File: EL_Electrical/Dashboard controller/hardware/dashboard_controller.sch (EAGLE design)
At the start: 46 parts, among them IC1 MCP2562-E_SN, IC2 MCP2515-I_SO, J1 22-27-2091-09, Q1 BSS138, Q4 BSS138, Q5 BSS138, Q6 BSS138

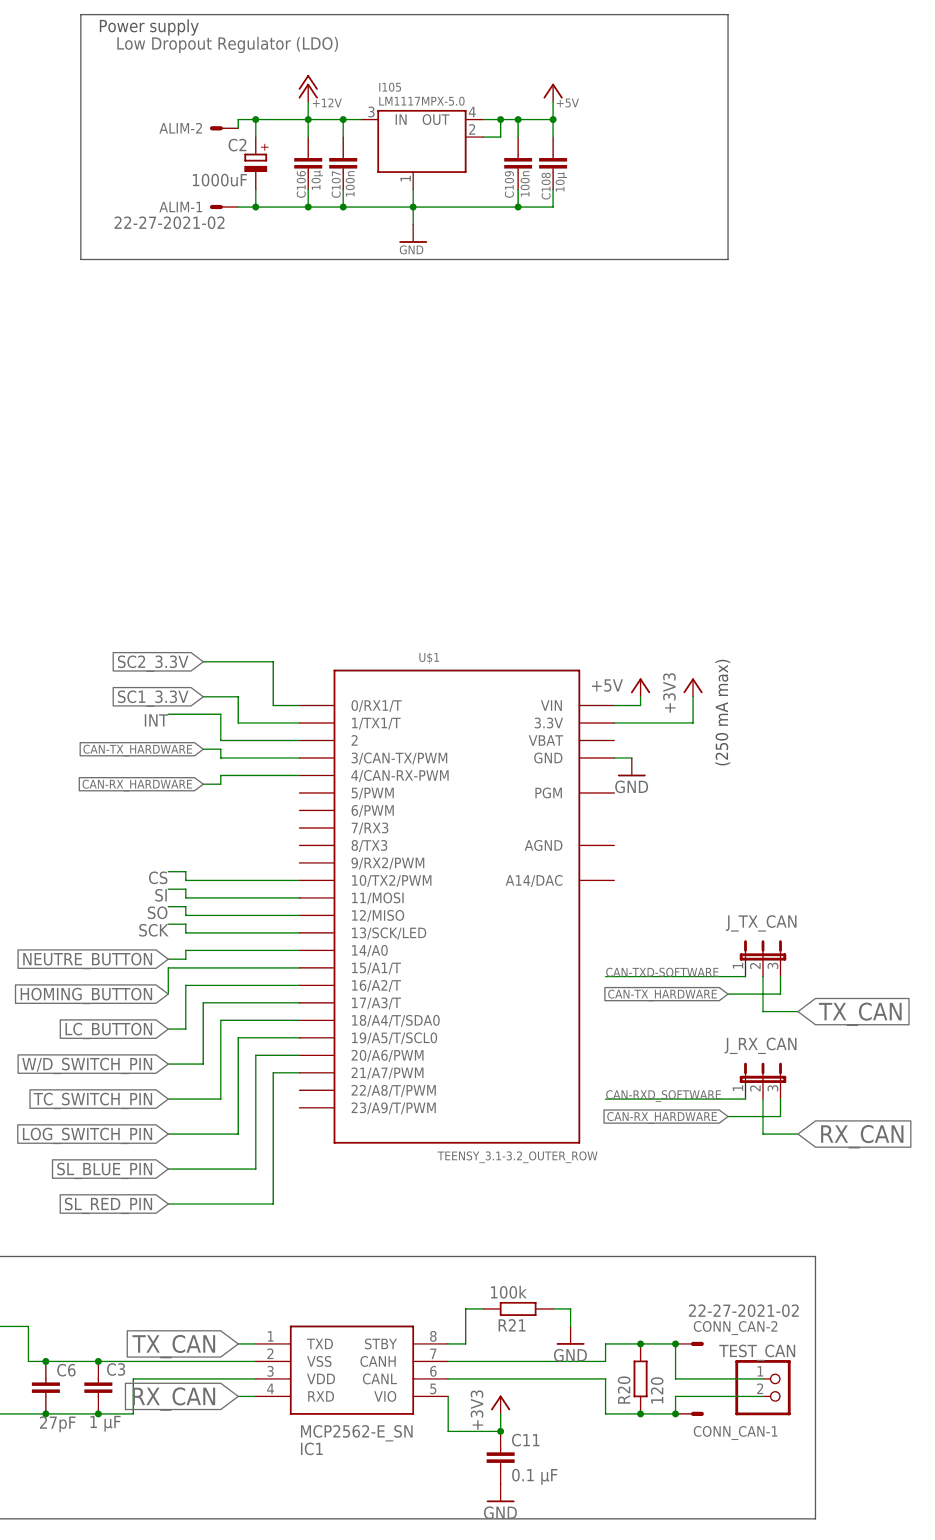
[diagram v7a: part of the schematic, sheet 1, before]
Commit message: Update holes and text
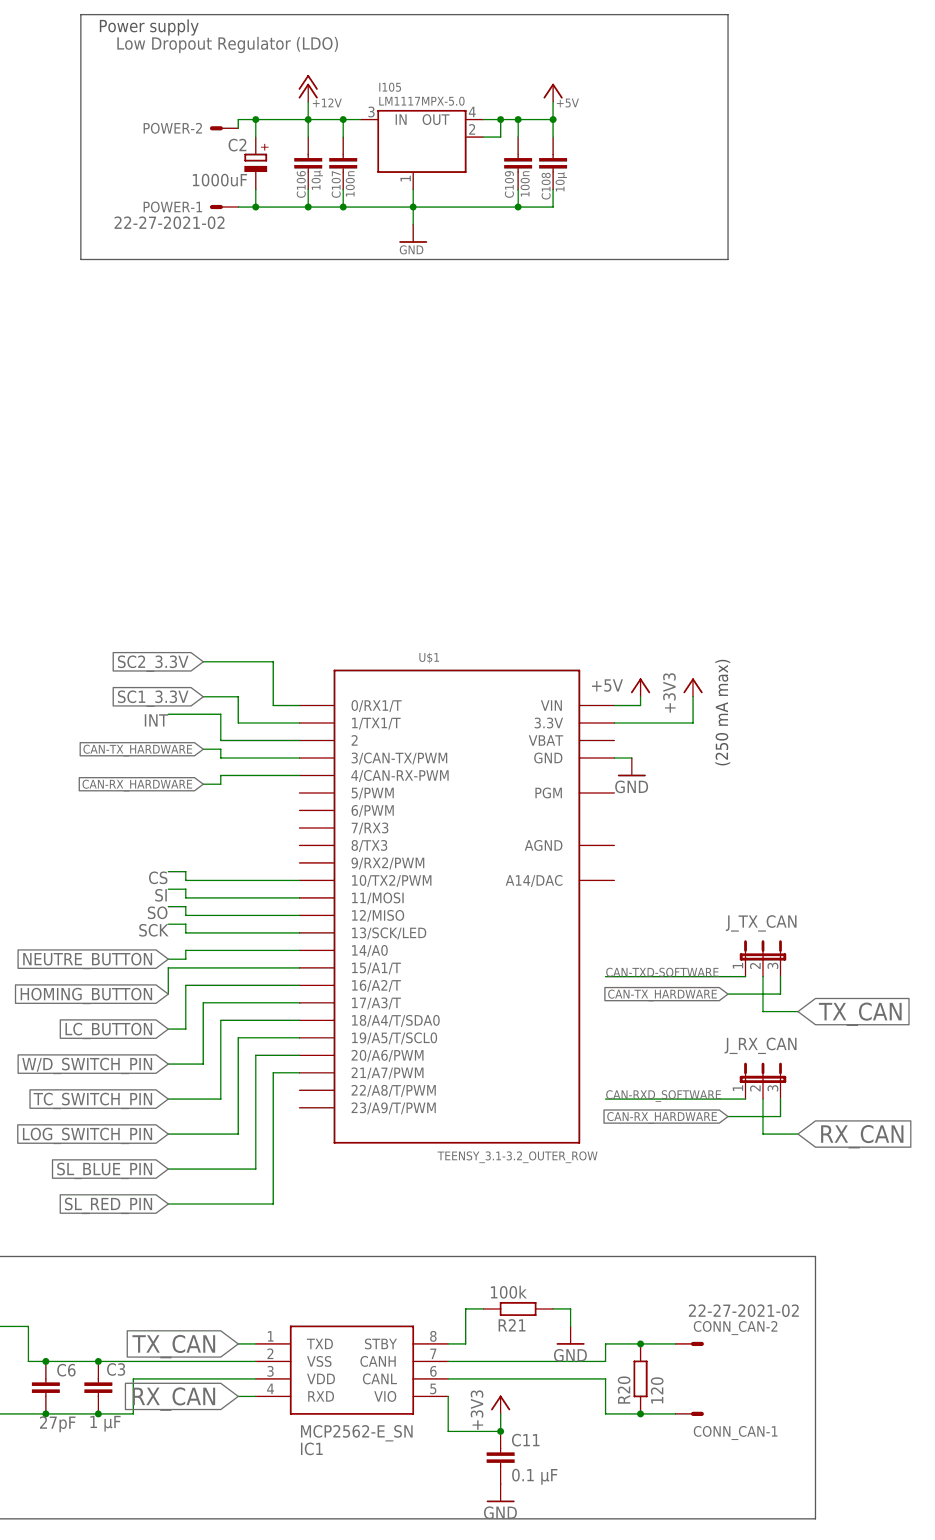
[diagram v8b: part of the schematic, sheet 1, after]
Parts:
- removed TEST_CAN: (no value), test_pin_DTA:PINHD-1X2
- renumbered ALIM to POWER
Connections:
- net N$1: no longer TEST_CAN.1
- net N$6: no longer TEST_CAN.2
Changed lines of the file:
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@@
 <part name="+3V6" library="supply1" library_urn="urn:adsk.eagle:library:371" deviceset="+3V3" device=""/>
 <part name="P+13" library="supply1" library_urn="urn:adsk.eagle:library:371" deviceset="+5V" device=""/>
-<part name="ALIM" library="con-molex" library_urn="urn:adsk.eagle:library:165" deviceset="22-?-02" device="27-2021" package3d_urn="urn:adsk.eagle:package:8078645/1"/>
+<part name="POWER" library="con-molex" library_urn="urn:adsk.eagle:library:165" deviceset="22-?-02" device="27-2021" package3d_urn="urn:adsk.eagle:package:8078645/1"/>
 <part name="R23" library="rcl" library_urn="urn:adsk.eagle:library:334" deviceset="R-EU_" device="R0805" package3d_urn="urn:adsk.eagle:package:23553/2" value="1k"/>
 <part name="+3V1" library="supply1" library_urn="urn:adsk.eagle:library:371" deviceset="+3V3" device=""/>
 <part name="GND" library="pinhead" library_urn="urn:adsk.eagle:library:325" deviceset="PINHD-1X1" device="" package3d_urn="urn:adsk.eagle:package:22485/2"/>
 <part name="GND2" library="supply1" deviceset="GND" device=""/>
-<part name="TEST_CAN" library="test_pin_DTA" deviceset="PINHD-1X2" device="" package3d_urn="urn:adsk.eagle:package:22435/2"/>
 <part name="Q1" library="transistor-small-signal" library_urn="urn:adsk.eagle:library:401" deviceset="BSS123" device="" package3d_urn="urn:adsk.eagle:package:28738/2" value="BSS138"/>
 <part name="R1" library="rcl" library_urn="urn:adsk.eagle:library:334" deviceset="R-EU_" device="R0805" package3d_urn="urn:adsk.eagle:package:23553/2" value="10k"/>
@@
 <attribute name="VALUE" x="190.5" y="200.66" size="1.778" layer="96" rot="R180"/>
 </instance>
-<instance part="ALIM" gate="-1" x="48.26" y="195.58" smashed="yes" rot="R180">
+<instance part="POWER" gate="-1" x="48.26" y="195.58" smashed="yes" rot="R180">
 <attribute name="NAME" x="45.72" y="196.342" size="1.524" layer="95" rot="R180"/>
 <attribute name="VALUE" x="49.022" y="194.183" size="1.778" layer="96" rot="R180"/>
 </instance>
-<instance part="ALIM" gate="-2" x="48.26" y="207.01" smashed="yes" rot="R180">
+<instance part="POWER" gate="-2" x="48.26" y="207.01" smashed="yes" rot="R180">
 <attribute name="NAME" x="45.72" y="207.772" size="1.524" layer="95" rot="R180"/>
 </instance>
@@
 <instance part="GND2" gate="1" x="234.95" y="11.43" smashed="yes">
 <attribute name="VALUE" x="232.41" y="8.89" size="1.778" layer="96"/>
-</instance>
-<instance part="TEST_CAN" gate="G$1" x="129.54" y="22.86" smashed="yes">
-<attribute name="NAME" x="120.65" y="28.575" size="1.778" layer="95"/>
-<attribute name="VALUE" x="123.19" y="17.78" size="1.778" layer="96"/>
 </instance>
 <instance part="Q1" gate="G$1" x="182.88" y="182.88" smashed="yes" rot="R270">
@@
 <pinref part="C2" gate="G$1" pin="+"/>
 <wire x1="53.34" y1="208.28" x2="53.34" y2="205.74" width="0.1524" layer="91"/>
-<pinref part="ALIM" gate="-2" pin="S"/>
+<pinref part="POWER" gate="-2" pin="S"/>
 <junction x="53.34" y="208.28"/>
 <wire x1="53.34" y1="208.28" x2="50.8" y2="208.28" width="0.1524" layer="91"/>
@@
 <pinref part="C108" gate="G$1" pin="2"/>
 <pinref part="C106" gate="G$1" pin="2"/>
-<pinref part="ALIM" gate="-1" pin="S"/>
+<pinref part="POWER" gate="-1" pin="S"/>
 <wire x1="60.96" y1="195.58" x2="53.34" y2="195.58" width="0.1524" layer="91"/>
 <junction x="60.96" y="195.58"/>
@@
 <wire x1="114.3" y1="20.32" x2="109.22" y2="20.32" width="0.1524" layer="91"/>
 <junction x="109.22" y="20.32"/>
-<wire x1="114.3" y1="20.32" x2="114.3" y2="22.86" width="0.1524" layer="91"/>
-<junction x="114.3" y="20.32"/>
-<pinref part="TEST_CAN" gate="G$1" pin="2"/>
-<wire x1="114.3" y1="22.86" x2="127" y2="22.86" width="0.1524" layer="91"/>
 </segment>
 </net>
@@
 <wire x1="114.3" y1="30.48" x2="109.22" y2="30.48" width="0.1524" layer="91"/>
 <junction x="109.22" y="30.48"/>
-<wire x1="114.3" y1="30.48" x2="114.3" y2="25.4" width="0.1524" layer="91"/>
-<junction x="114.3" y="30.48"/>
-<pinref part="TEST_CAN" gate="G$1" pin="1"/>
-<wire x1="127" y1="25.4" x2="114.3" y2="25.4" width="0.1524" layer="91"/>
-</segment>
-</net>
+</segment>
+</net>
